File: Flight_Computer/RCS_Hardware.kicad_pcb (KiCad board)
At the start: 2 copper layers, 60 x 53.1 mm, 55 parts, among them J1 SWD, J2 TYPE-C-31-M-12, J3 SPI, J4 5V, J5 GND, J6 Solenoids, J7 SPI, J8 Conn_01x05_Male, U1 STM32F401CCU6, U2 AMS1117-3.3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

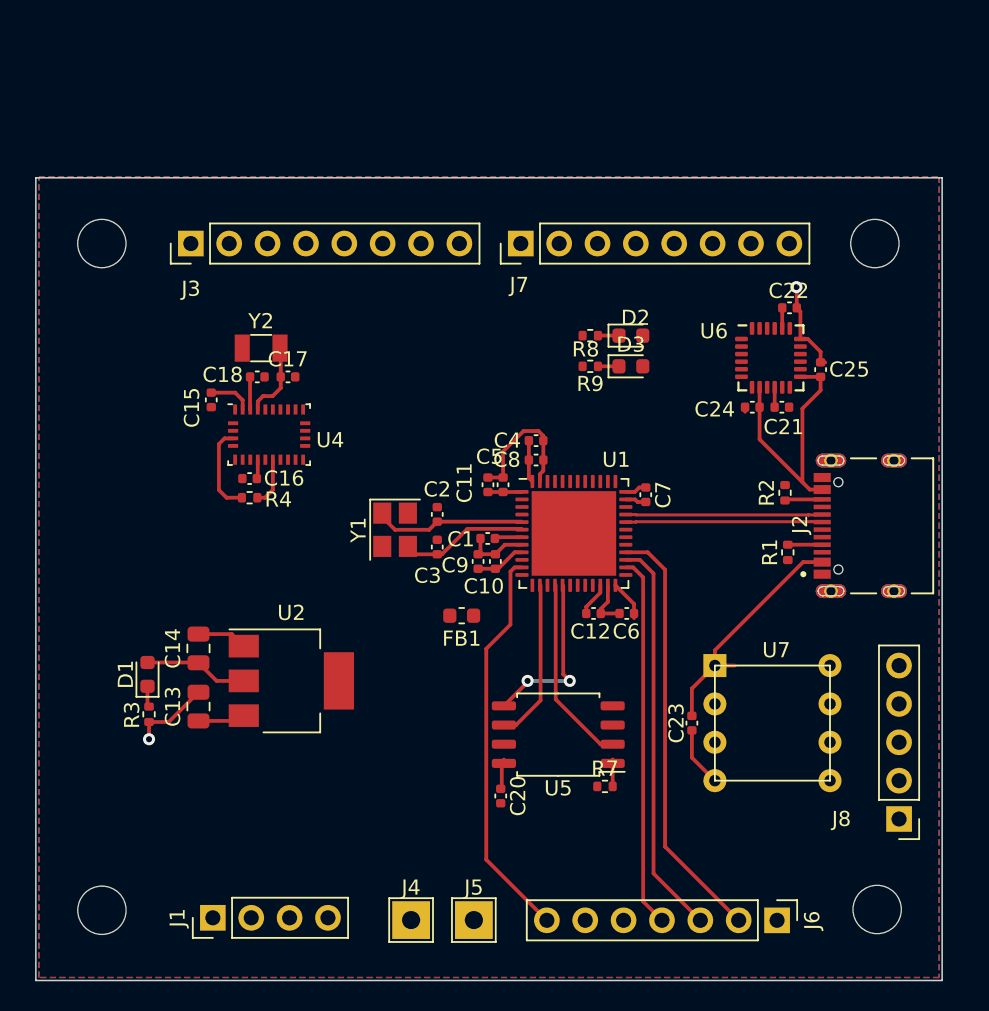
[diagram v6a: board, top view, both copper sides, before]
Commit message: Everthing is routed
ONLY errors/warnings for USB-C footprint and Ethan's awesome differential driver footprint.
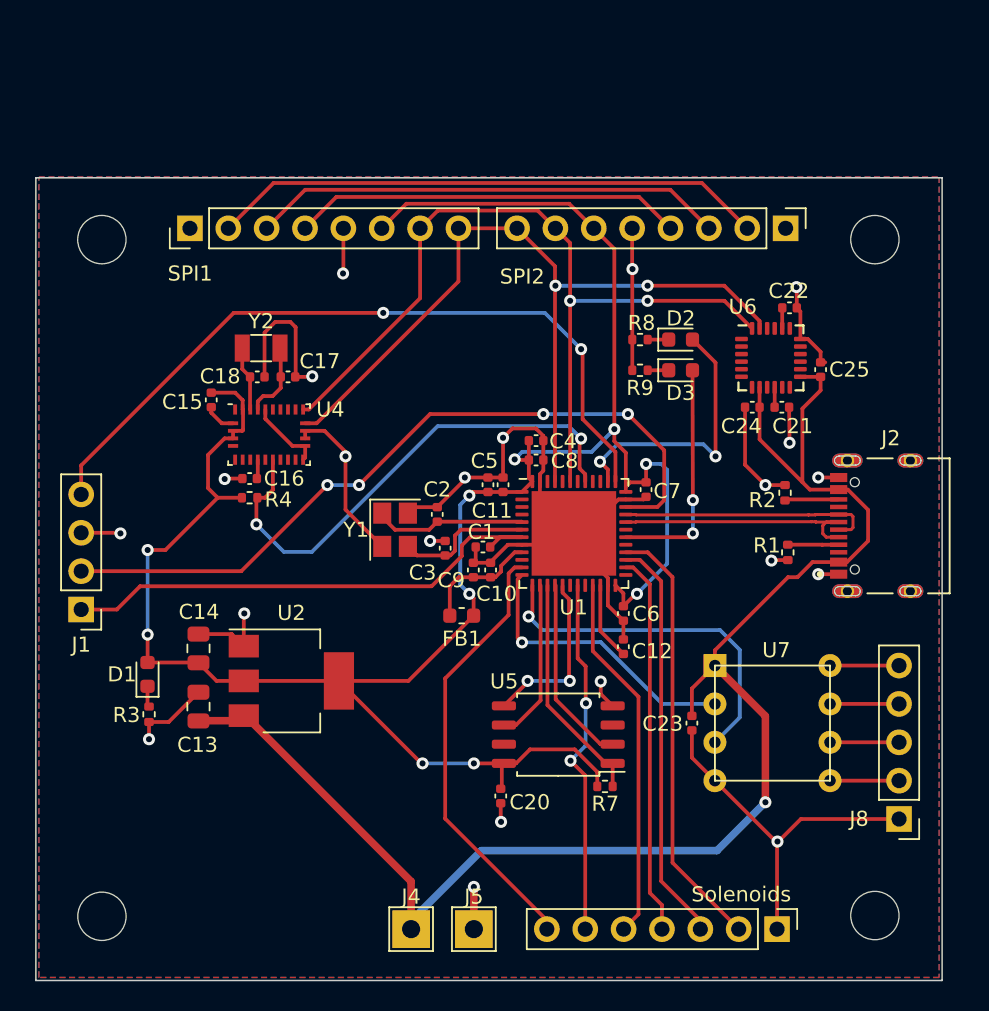
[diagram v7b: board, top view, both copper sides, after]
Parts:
- moved J1 22.2 mm to (104.6, 104.2), turned to 180 degrees
- moved SPI2 17.6 mm to (151.2, 79.0), turned to -90 degrees
- moved D2 3.30 mm to (144.3, 86.4)
- moved D3 3.30 mm to (144.3, 88.4)
- moved R8 3.30 mm to (141.6, 86.4)
- moved R9 3.30 mm to (141.6, 88.4)
- moved C12 2.96 mm to (140.5, 106.7), turned to 90 degrees
- moved J2 1.09 mm to (159.5, 98.7)
- moved SPI1 1.01 mm to (111.8, 79.0)
- moved C1 0.65 mm to (131.2, 100.1)
- moved C10 0.65 mm to (131.7, 101.6)
- moved C9 0.65 mm to (130.6, 101.6)
- moved J4 0.60 mm to (126.4, 125.4)
- moved J5 0.60 mm to (130.6, 125.4)
- moved Solenoids 0.58 mm to (150.7, 125.4)
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- renumbered J3 to SPI1, J7 to SPI2, J6 to Solenoids
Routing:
- net +3.3V: track 26.7 -> 146.8 mm, vias 0 -> 10
- net GND: track 37.3 -> 145.5 mm, vias 2 -> 21
- net VBUS: track 36.9 -> 102.4 mm, vias 0 -> 1
- net /SDA: track 0.00 -> 55.5 mm, vias 0 -> 2
- net /SCL: track 0.00 -> 54.2 mm, vias 0 -> 2
- net /SWDIO: track 0.00 -> 50.2 mm, vias 0 -> 4
- net /SWCLK: track 0.00 -> 49.9 mm, vias 0 -> 2
- net /MOSI2: track 0.00 -> 36.8 mm
- net /NRST: track 1.82 -> 34.0 mm
- net /MISO2: track 0.00 -> 31.4 mm
- net /BNO_NRST: track 3.24 -> 34.1 mm, vias 0 -> 2
- net /SCK: track 0.00 -> 25.9 mm
- net /S3: track 0.00 -> 24.4 mm
- net /TX: track 0.00 -> 23.9 mm, vias 0 -> 1
- net /S2: track 0.00 -> 23.2 mm, vias 0 -> 2
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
